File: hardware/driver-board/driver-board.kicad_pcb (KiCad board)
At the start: 4 copper layers, 42.2 x 36.8 mm, 56 parts, among them J1 Conn_01x13_Male, U1 TXS0108E, U2 ME6210, U3 ME6210, U4 TLV61046ADB, U5 NC7SZ125, U6 FT813, U7 ER-TFT040-2, X1 YSX321SL

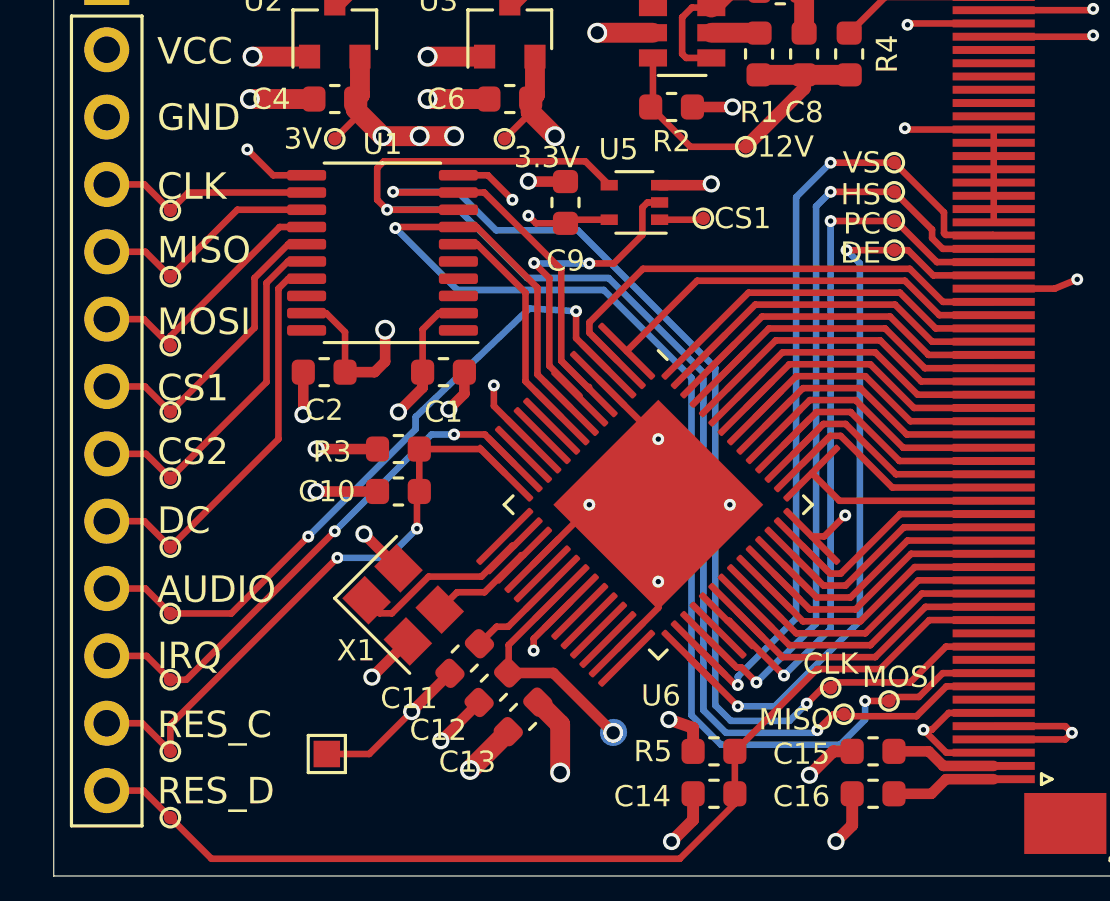
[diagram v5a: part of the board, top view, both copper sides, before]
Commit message: Adapt new SPI signal names from OSHWA
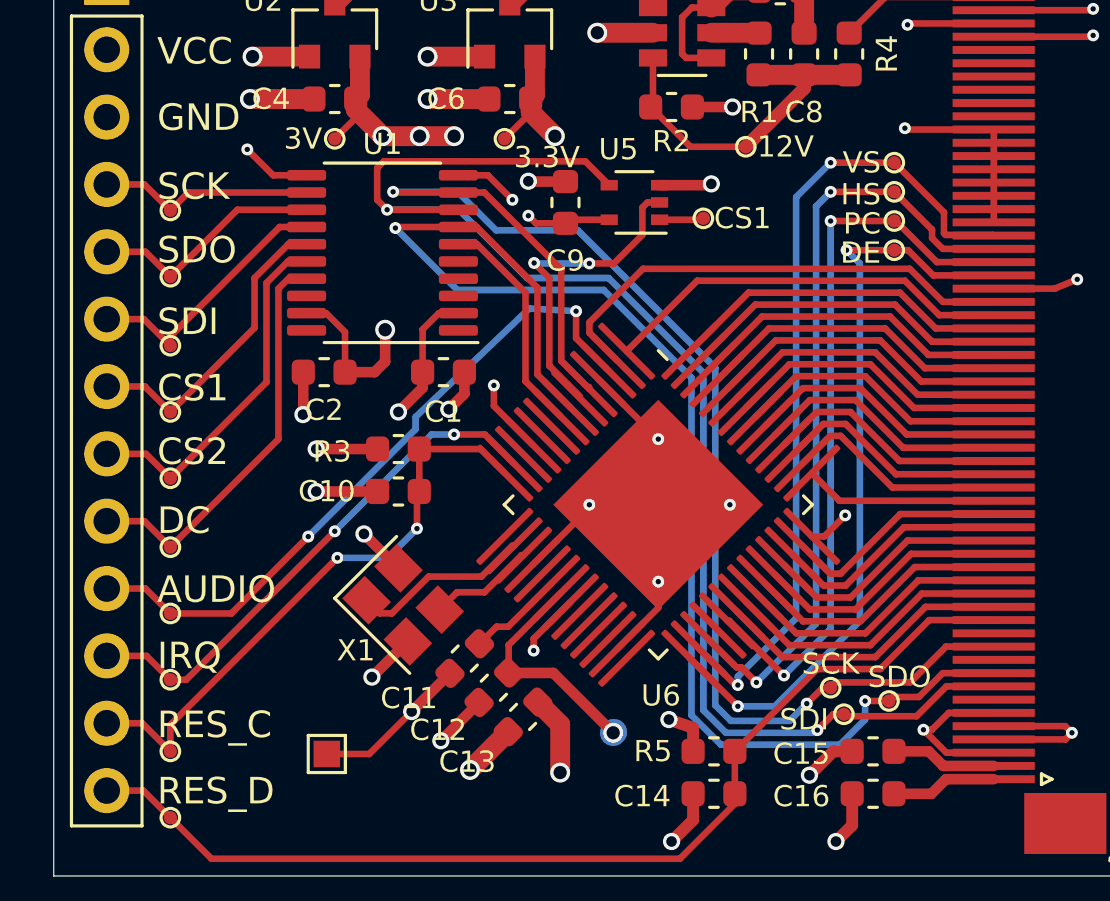
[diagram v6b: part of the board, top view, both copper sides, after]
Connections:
- net CLK renamed SCK
- net CLK_3V renamed SCK_3V
- net MISO renamed SDI
- net MISO_3V renamed SDI_3V
- net MISO_BUFFER renamed SDI_BUFFER
- net MOSI renamed SDO
- net MOSI_3V renamed SDO_3V
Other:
- board text added: "SCK"
- board text added: "SDI"
- board text added: "SDO"
- board text removed: "CLK"
- board text removed: "MISO"
- board text removed: "MOSI"

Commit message: Add hw license and finalize routing
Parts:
- added REF**: OSHW-Logo_5.7x6mm_SilkScreen, Symbol:OSHW-Logo_5.7x6mm_SilkScreen, B.Cu at (132.4, 62.2)
- moved TP11 6.16 mm to (128.4, 83.2)
- moved TP13 5.96 mm to (130.9, 83.2)
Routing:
- net CS2_3V: track 0.00 -> 59.6 mm, vias 0 -> 3
- net DC_3V: track 0.00 -> 56.3 mm, vias 0 -> 3
- net CS1_3V: track 10.2 -> 29.8 mm, vias 0 -> 2
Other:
- board text added: "Copyright © Raphael Stäbler"
- board text added: "Licensed under CERN-OHL-S v2"
- board text added: "https://github.com/blazer82/FT81x_Arduino_Driver"

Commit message: Improve and fix pcb and schematic
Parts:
- moved TP1 4.32 mm to (140.2, 55.4)
- moved R4 1.65 mm to (140.1, 52.1)
- turned C8 to 270 degrees
- turned R1 to 270 degrees
- turned R2 to 180 degrees
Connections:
- R2 pad 1: +12V -> Net-(R1-Pad2)
- U4 pad 3: +12V -> Net-(R1-Pad2)
- U4 pad 5: Net-(R1-Pad2) -> +12V
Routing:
- net +12V: track 13.1 -> 7.42 mm
- net +3V3: track 37.0 -> 41.2 mm
- net Net-(R1-Pad2): track 1.81 -> 5.48 mm
- net GND: track 107.2 -> 110.5 mm, vias 34 -> 39
- net +3V0: track 45.0 -> 48.1 mm, vias 12 -> 14
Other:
- board text added: "REV2007D"
